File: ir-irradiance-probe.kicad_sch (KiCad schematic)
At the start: 40 parts, among them J2 SM04B-SRSS-TB-LF-SN, J3 PinHeader_1x2_P2.54mm_Drill1.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

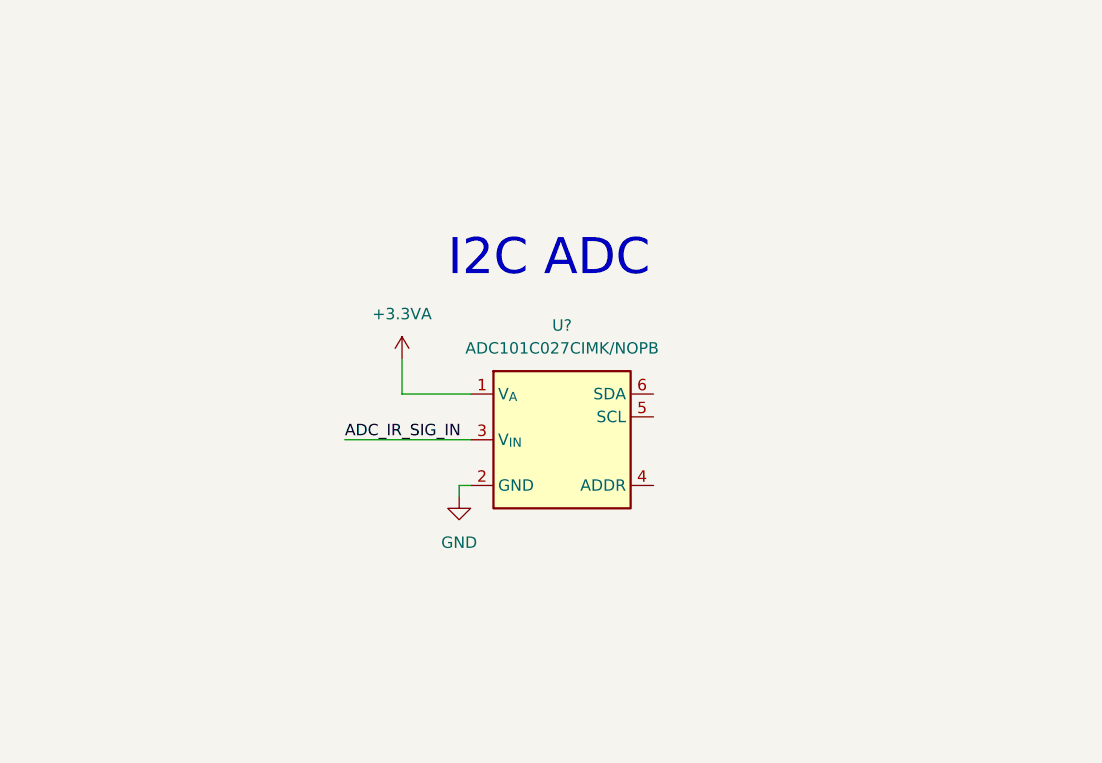
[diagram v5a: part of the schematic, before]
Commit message: [#47284] Complete circuit for I2C ADC
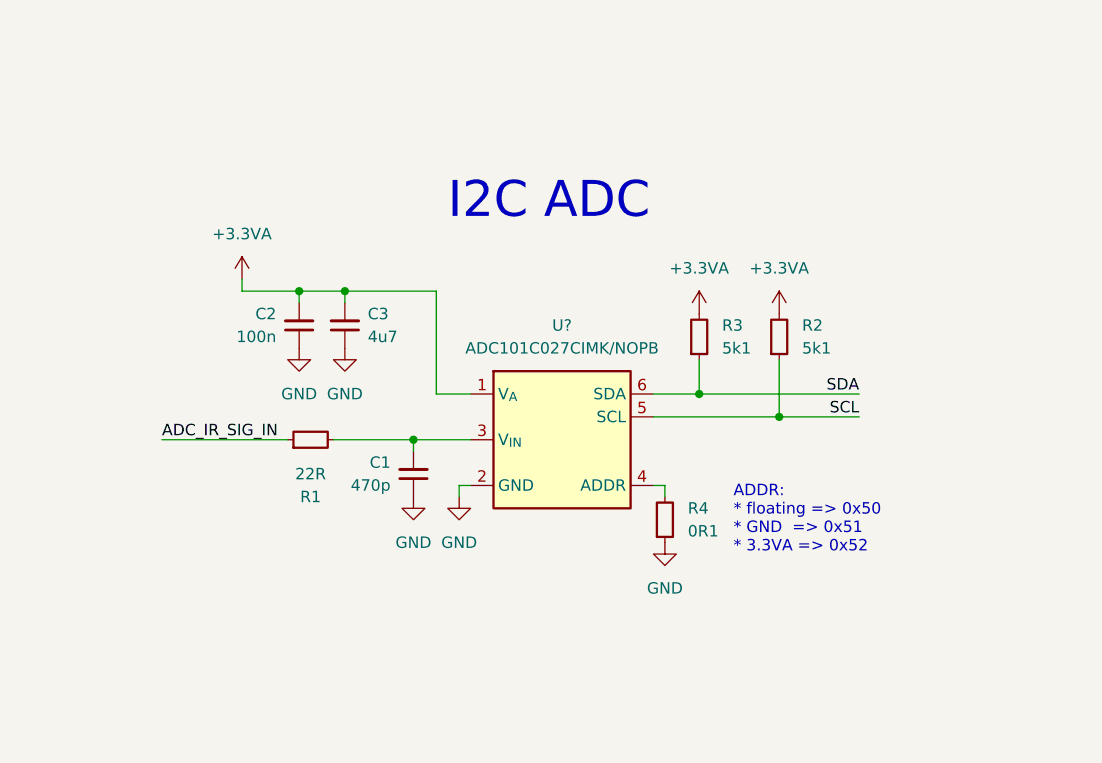
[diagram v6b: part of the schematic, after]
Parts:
- added C1: C_470p_0402, antmicro-footprints:C_0402_1005Metric, symbol Capacitors0402:C_470p_0402
- added C2: C_100n_0402, antmicro-footprints:C_0402_1005Metric, symbol Capacitors0402:C_100n_0402
- added C3: C_4u7_0603, antmicro-footprints:C_0603_1608Metric, symbol Capacitors0603:C_4u7_0603
- added R1: R_22R_0402, antmicro-footprints:R_0402_1005Metric, symbol Resistors0402:R_22R_0402
- added R2, R3: R_5k1_0402, antmicro-footprints:R_0402_1005Metric, symbol Resistors0402:R_5k1_0402
- added R4: R_0R1_0402, antmicro-footprints:R_0402_1005Metric, symbol Resistors0402:R_0R1_0402
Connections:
- net +3.3VA: now also C2.2, C3.2, R2.2, R3.2
- net ADC_IR_SIG_IN: now also R1.1; no longer U?.3 (V_{IN})
- net GND: now also C1.1, C2.1, C3.1, R4.1
- net SCL: now also U?.5 (SCL), R2.1
- net SDA: now also U?.6 (SDA), R3.1
- net at U?.4 (ADDR): now also R4.2
- new net: C1.2, R1.2, U?.3 (V_{IN})
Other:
- note added: "ADDR: * floating => 0x50 * GND => 0x51 * 3.3VA => 0x52"

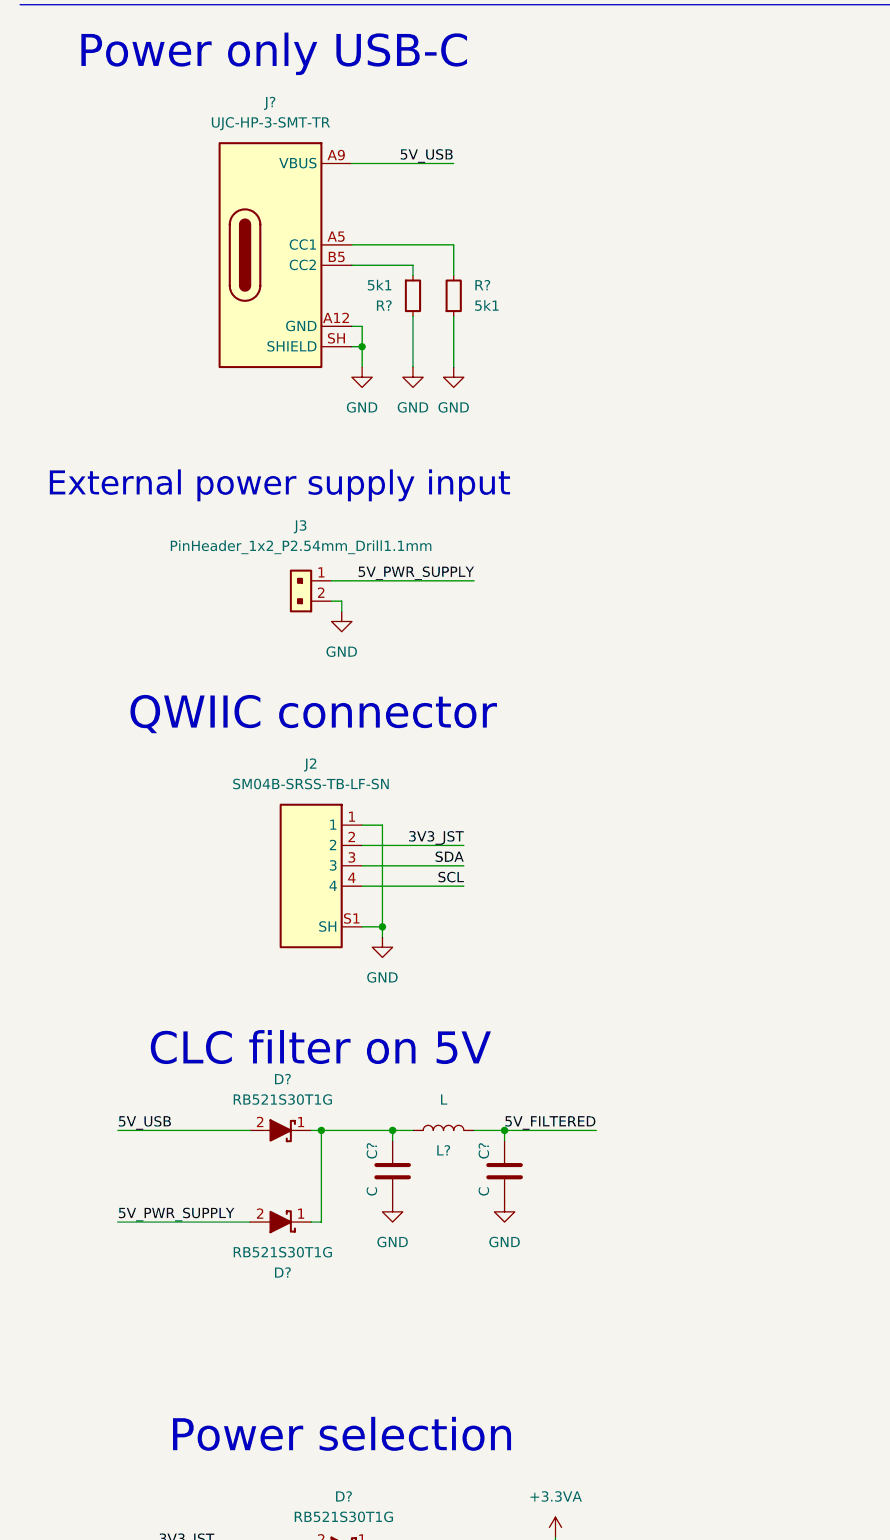
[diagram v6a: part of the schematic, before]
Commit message: [#47284] Add TVS diodes on USB-C and QWIIC connectors
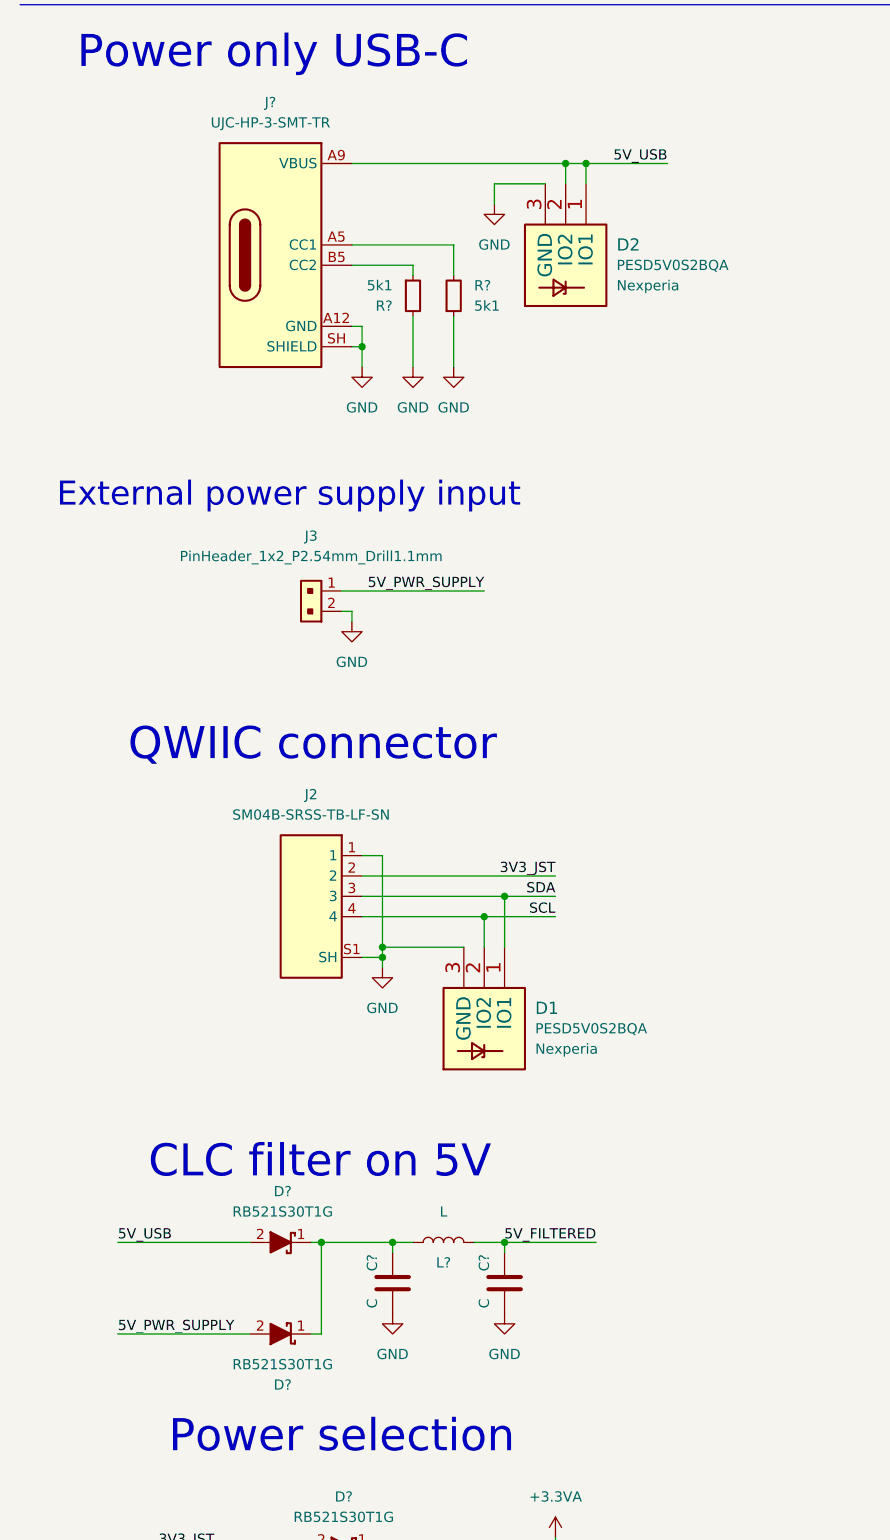
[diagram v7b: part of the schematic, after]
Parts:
- added D1, D2: PESD5V0S2BQA, antmicro-footprints:TPD2E009DRTR, symbol TVSDiodes:PESD5V0S2BQA
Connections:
- net 5V_USB: now also D2.1 (IO1), D2.2 (IO2)
- net GND: now also D1.3 (GND), D2.3 (GND)
- net SCL: now also D1.2 (IO2)
- net SDA: now also D1.1 (IO1)
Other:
- moved on the sheet: C?, D?, J2, J3, L?

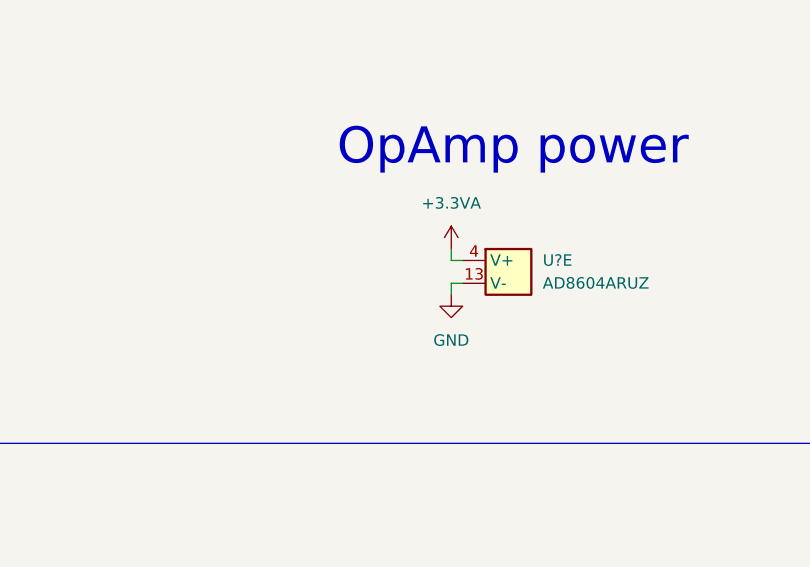
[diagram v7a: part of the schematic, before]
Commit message: [#47284] Add 100n capacitor on OpAmp power pin
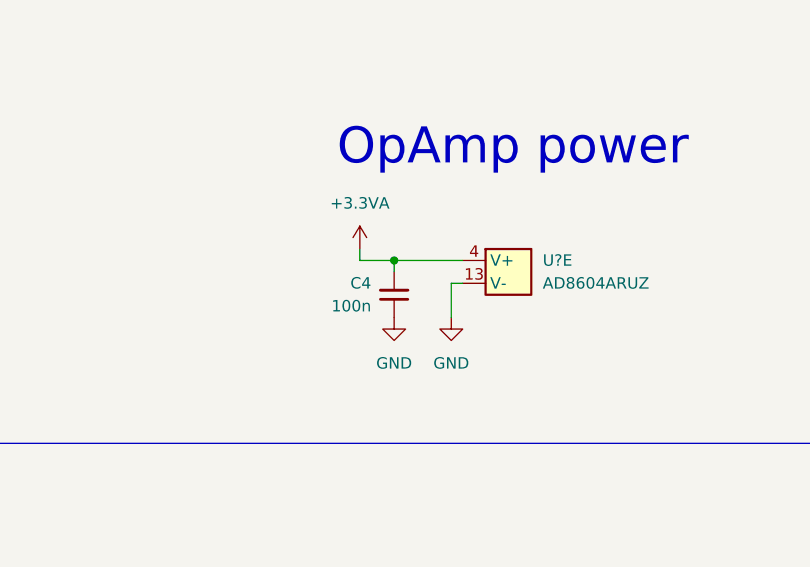
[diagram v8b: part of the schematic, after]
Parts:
- added C4: C_100n_0402, antmicro-footprints:C_0402_1005Metric, symbol Capacitors0402:C_100n_0402
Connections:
- net +3.3VA: now also C4.2
- net GND: now also C4.1
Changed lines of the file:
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@@
   (junction (at 307.34 227.33) (diameter 0) (color 0 0 0 0)
   )
+  (junction (at 139.7 232.41) (diameter 0) (color 0 0 0 0)
+  )
   (junction (at 308.61 111.76) (diameter 0) (color 0 0 0 0)
   )
@@
     (stroke (width 0) (type default))
   )
+  (wire (pts (xy 139.7 232.41) (xy 139.7 233.68))
+    (stroke (width 0) (type default))
+  )
   (wire (pts (xy 67.31 231.14) (xy 78.74 231.14))
     (stroke (width 0) (type default))
@@
     (stroke (width 0) (type default))
   )
-  (wire (pts (xy 146.05 236.22) (xy 146.05 234.95))
+  (wire (pts (xy 146.05 234.95) (xy 146.05 238.76))
     (stroke (width 0) (type default))
   )
@@
     (stroke (width 0) (type default))
   )
+  (wire (pts (xy 139.7 232.41) (xy 147.32 232.41))
+    (stroke (width 0) (type default))
+  )
   (wire (pts (xy 327.66 53.34) (xy 334.01 53.34))
     (stroke (width 0) (type default))
@@
     (stroke (width 0) (type default))
   )
-  (wire (pts (xy 146.05 232.41) (xy 146.05 231.14))
+  (wire (pts (xy 135.89 232.41) (xy 135.89 231.14))
     (stroke (width 0) (type default))
   )
@@
     (stroke (width 0) (type default))
   )
-  (wire (pts (xy 147.32 232.41) (xy 146.05 232.41))
+  (wire (pts (xy 135.89 232.41) (xy 139.7 232.41))
     (stroke (width 0) (type default))
   )
@@
     )
   )
+  (symbol (lib_id "Capacitors0402:C_100n_0402") (at 139.7 238.76 270) (mirror x) (unit 1)
+    (in_bom yes) (on_board yes) (dnp no)
+    (property "Reference" "C4" (at 137.16 234.9436 90)
+      (effects (font (size 1.27 1.27) (thickness 0.15)) (justify right))
+    )
+    (property "Value" "C_100n_0402" (at 129.54 218.44 0)
+      (effects (font (size 1.27 1.27) (thickness 0.15)) (justify left bottom) hide)
+    )
+    (property "Footprint" "antmicro-footprints:C_0402_1005Metric" (at 127 218.44 0)
+      (effects (font (size 1.27 1.27) (thickness 0.15)) (justify left bottom) hide)
+    )
+    (property "Datasheet" "https://search.murata.co.jp/Ceramy/image/img/A01X/G101/ENG/GRM155R61H104KE14-01.pdf" (at 124.46 218.44 0)
+      (effects (font (size 1.27 1.27) (thickness 0.15)) (justify left bottom) hide)
+    )
+    (property "MPN" "GRM155R61H104KE14D" (at 121.92 218.44 0)
+      (effects (font (size 1.27 1.27) (thickness 0.15)) (justify left bottom) hide)
+    )
+    (property "Manufacturer" "Murata" (at 119.38 218.44 0)
+      (effects (font (size 1.27 1.27) (thickness 0.15)) (justify left bottom) hide)
+    )
+    (property "License" "Apache-2.0" (at 116.84 218.44 0)
+      (effects (font (size 1.27 1.27) (thickness 0.15)) (justify left bottom) hide)
+    )
+    (property "Author" "Antmicro" (at 114.3 218.44 0)
+      (effects (font (size 1.27 1.27) (thickness 0.15)) (justify left bottom) hide)
+    )
+    (property "Val" "100n" (at 137.16 237.4836 90)
+      (effects (font (size 1.27 1.27) (thickness 0.15)) (justify right))
+    )
+    (property "Voltage" "50V" (at 111.76 218.44 0)
+      (effects (font (size 1.27 1.27)) (justify left bottom) hide)
+    )
+    (property "Dielectric" "X5R" (at 109.22 218.44 0)
+      (effects (font (size 1.27 1.27)) (justify left bottom) hide)
+    )
+    (pin "1")
+    (pin "2")
+    (instances
+      (project "ir-irradiance-probe"
+        (path "/97d94a71-0b57-4bb1-ae37-779338f5fb57"
+          (reference "C4") (unit 1)
+        )
+      )
+    )
+  )
   (symbol (lib_id "antmicroMechanicalParts:PCB_Mount_Hole_2.5_6.2") (at 266.7 278.13 0) (unit 1)
     (in_bom no) (on_board yes) (dnp no) (fields_autoplaced)
@@
     )
   )
+  (symbol (lib_id "antmicropower:GND") (at 139.7 238.76 0) (unit 1)
+    (in_bom yes) (on_board yes) (dnp no) (fields_autoplaced)
+    (property "Reference" "#PWR08" (at 148.59 241.3 0)
+      (effects (font (size 1.27 1.27) (thickness 0.15)) (justify left bottom) hide)
+    )
+    (property "Value" "GND" (at 139.7 243.84 0)
+      (effects (font (size 1.27 1.27) (thickness 0.15)))
+    )
+    (property "Footprint" "" (at 148.59 246.38 0)
+      (effects (font (size 1.27 1.27) (thickness 0.15)) (justify left bottom) hide)
+    )
+    (property "Datasheet" "" (at 148.59 251.46 0)
+      (effects (font (size 1.27 1.27) (thickness 0.15)) (justify left bottom) hide)
+    )
+    (property "Author" "Antmicro" (at 148.59 246.38 0)
+      (effects (font (size 1.27 1.27) (thickness 0.15)) (justify left bottom) hide)
+    )
+    (property "License" "Apache-2.0" (at 148.59 248.92 0)
+      (effects (font (size 1.27 1.27) (thickness 0.15)) (justify left bottom) hide)
+    )
+    (pin "1")
+    (instances
+      (project "ir-irradiance-probe"
+        (path "/97d94a71-0b57-4bb1-ae37-779338f5fb57"
+          (reference "#PWR08") (unit 1)
+        )
+      )
+    )
+  )
   (symbol (lib_id "antmicropower:GND") (at 158.75 118.11 0) (unit 1)
     (in_bom yes) (on_board yes) (dnp no) (fields_autoplaced)
@@
     )
   )
-  (symbol (lib_id "antmicropower:+3.3VA") (at 146.05 231.14 0) (unit 1)
-    (in_bom yes) (on_board yes) (dnp no) (fields_autoplaced)
-    (property "Reference" "#PWR?" (at 146.05 234.95 0)
+  (symbol (lib_id "antmicropower:+3.3VA") (at 135.89 231.14 0) (unit 1)
+    (in_bom yes) (on_board yes) (dnp no) (fields_autoplaced)
+    (property "Reference" "#PWR?" (at 135.89 234.95 0)
       (effects (font (size 1.27 1.27)) hide)
     )
-    (property "Value" "+3.3VA" (at 146.05 226.06 0)
+    (property "Value" "+3.3VA" (at 135.89 226.06 0)
       (effects (font (size 1.27 1.27)))
     )
-    (property "Footprint" "" (at 146.05 231.14 0)
+    (property "Footprint" "" (at 135.89 231.14 0)
       (effects (font (size 1.27 1.27)) hide)
     )
-    (property "Datasheet" "" (at 146.05 231.14 0)
+    (property "Datasheet" "" (at 135.89 231.14 0)
       (effects (font (size 1.27 1.27)) hide)
     )
@@
     )
   )
-  (symbol (lib_id "antmicropower:GND") (at 146.05 236.22 0) (unit 1)
-    (in_bom yes) (on_board yes) (dnp no) (fields_autoplaced)
-    (property "Reference" "#PWR?" (at 154.94 238.76 0)
-      (effects (font (size 1.27 1.27) (thickness 0.15)) (justify left bottom) hide)
-    )
-    (property "Value" "GND" (at 146.05 241.3 0)
-      (effects (font (size 1.27 1.27) (thickness 0.15)))
-    )
-    (property "Footprint" "" (at 154.94 243.84 0)
-      (effects (font (size 1.27 1.27) (thickness 0.15)) (justify left bottom) hide)
-    )
-    (property "Datasheet" "" (at 154.94 248.92 0)
-      (effects (font (size 1.27 1.27) (thickness 0.15)) (justify left bottom) hide)
-    )
-    (property "Author" "Antmicro" (at 154.94 243.84 0)
-      (effects (font (size 1.27 1.27) (thickness 0.15)) (justify left bottom) hide)
-    )
-    (property "License" "Apache-2.0" (at 154.94 246.38 0)
-      (effects (font (size 1.27 1.27) (thickness 0.15)) (justify left bottom) hide)
-    )
+  (symbol (lib_id "antmicropower:GND") (at 146.05 238.76 0) (unit 1)
+    (in_bom yes) (on_board yes) (dnp no) (fields_autoplaced)
+    (property "Reference" "#PWR?" (at 154.94 241.3 0)
+      (effects (font (size 1.27 1.27) (thickness 0.15)) (justify left bottom) hide)
+    )
+    (property "Value" "GND" (at 146.05 243.84 0)
+      (effects (font (size 1.27 1.27) (thickness 0.15)))
+    )
+    (property "Footprint" "" (at 154.94 246.38 0)
+      (effects (font (size 1.27 1.27) (thickness 0.15)) (justify left bottom) hide)
+    )
+    (property "Datasheet" "" (at 154.94 251.46 0)
+      (effects (font (size 1.27 1.27) (thickness 0.15)) (justify left bottom) hide)
+    )
+    (property "Author" "Antmicro" (at 154.94 246.38 0)
+      (effects (font (size 1.27 1.27) (thickness 0.15)) (justify left bottom) hide)
+    )
+    (property "License" "Apache-2.0" (at 154.94 248.92 0)
+      (effects (font (size 1.27 1.27) (thickness 0.15)) (justify left bottom) hide)
+    )
